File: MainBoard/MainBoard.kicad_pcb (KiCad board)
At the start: 2 copper layers, 55 x 90 mm, 160 parts, among them CN3 PJ-342, J1 1769, Q3 MMBT2222ALT1G, SW1 TS3735A 250GF 030, SW2 TS3735A 250GF 030, SW3 TS3735A 250GF 030, SW4 TS3735A 250GF 030, SW5 TS3735A 250GF 030, U1 V3S, U10 F35SQA512M-WWT, U11 XC6206P302MR_C5148691, U2 ESP32-MINI-1-H4, U3 SGTL5000XNAA3R2, U4 BQ27220YZFR, U6 EA3036C, U7 MT3608, U8 PCM1807PW, U9 BQ24074RGTR, X1 FC-12M32.768KHZ7PF20PPM, X2 X322524MOB4SI, X3 AFC01-S45FCA-00

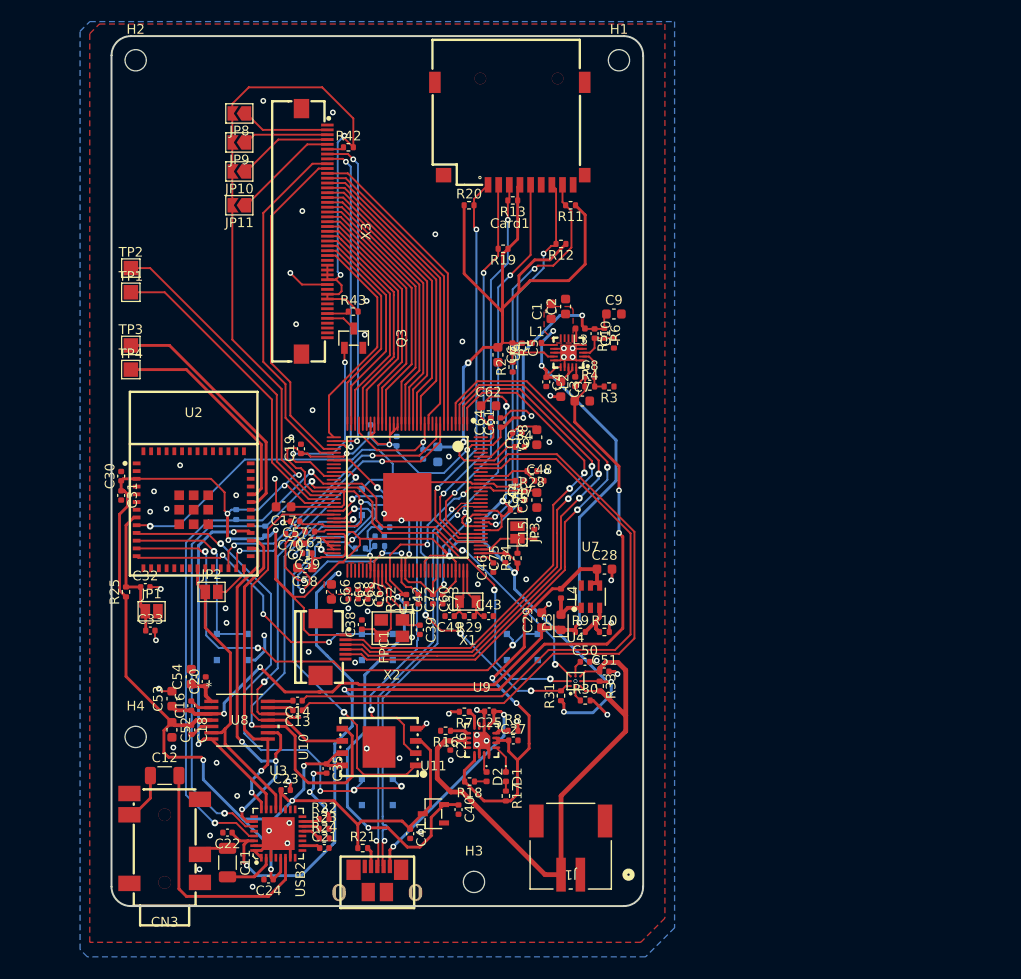
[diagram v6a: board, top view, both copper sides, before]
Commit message: cleaned up silkscreen
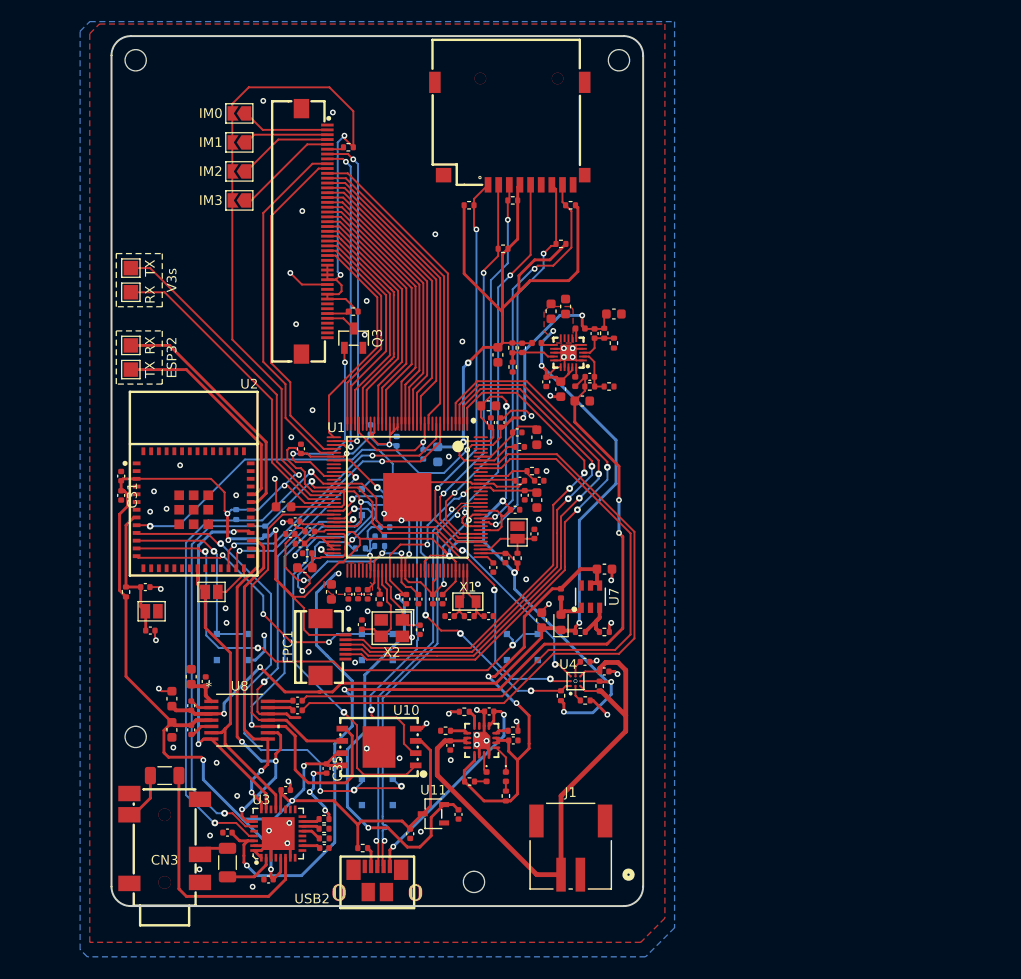
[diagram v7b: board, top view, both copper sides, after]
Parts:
- moved C40 0.50 mm to (158.4, 115.5)
- moved JP11 0.50 mm to (135.7, 52.0)
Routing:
- net VSYS: track 48.1 -> 48.7 mm
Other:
- board text added: "ESP32"
- board text added: "IM0"
- board text added: "IM1"
- board text added: "IM2"
- board text added: "IM3"
- board text added: "RX"
- board text added: "TX"
- board text added: "V3s"

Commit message: added teardrops and voltage probe points
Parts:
- added TP5: TestPoint, TestPoint:TestPoint_Pad_1.5x1.5mm, F.Cu at (124.5, 54.0)
- added TP6: TestPoint, TestPoint:TestPoint_Pad_1.5x1.5mm, F.Cu at (124.5, 51.0)
- added TP7: TestPoint, TestPoint:TestPoint_Pad_1.5x1.5mm, F.Cu at (124.5, 48.0)
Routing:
- net +5V: track 93.9 -> 168.2 mm
- net +3.3V: track 450.6 -> 461.5 mm
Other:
- board text added: "3.3V"
- board text added: "5V"
- board text added: "GND"
- board text added: "IO0"
- board text added: "RESET"
